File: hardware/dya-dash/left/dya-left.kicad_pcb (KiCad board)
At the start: 2 copper layers, 127.2 x 92.9 mm, 115 parts

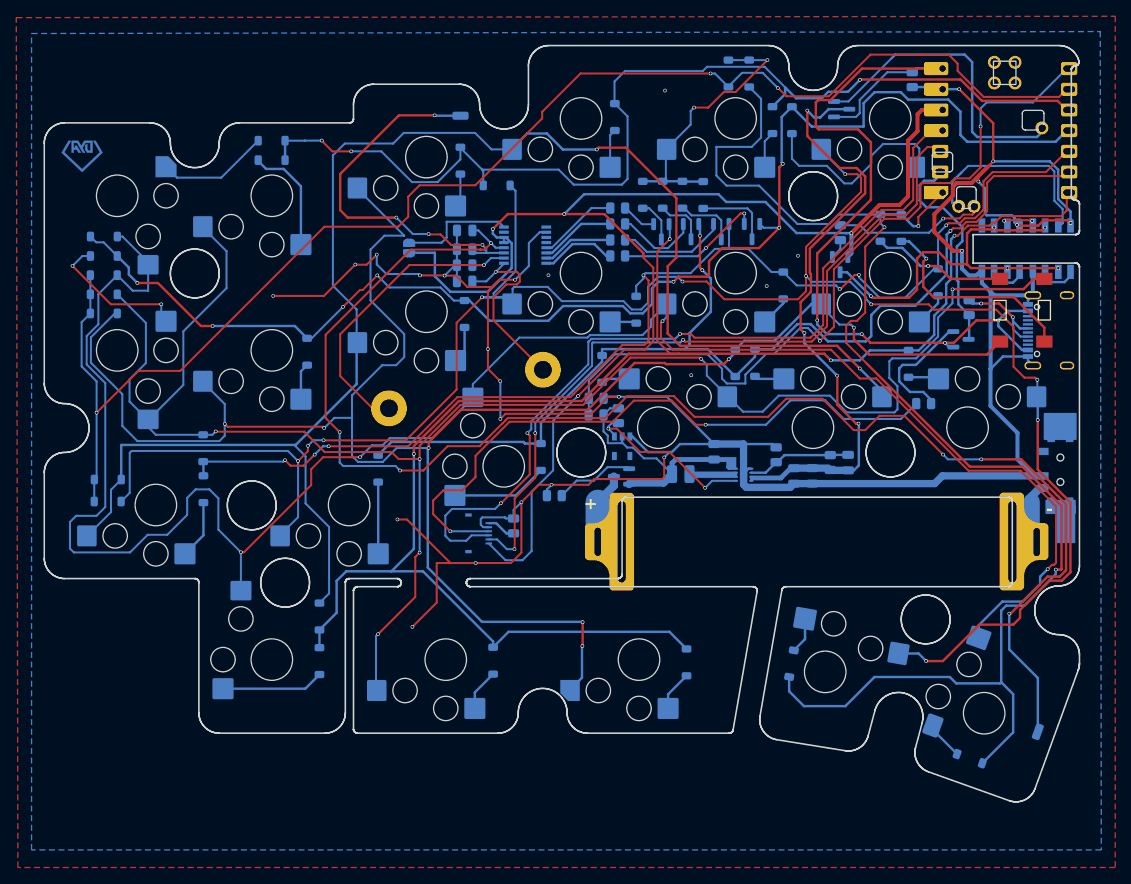
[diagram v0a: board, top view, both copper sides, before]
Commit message: Change FFC connector direction for arrow model
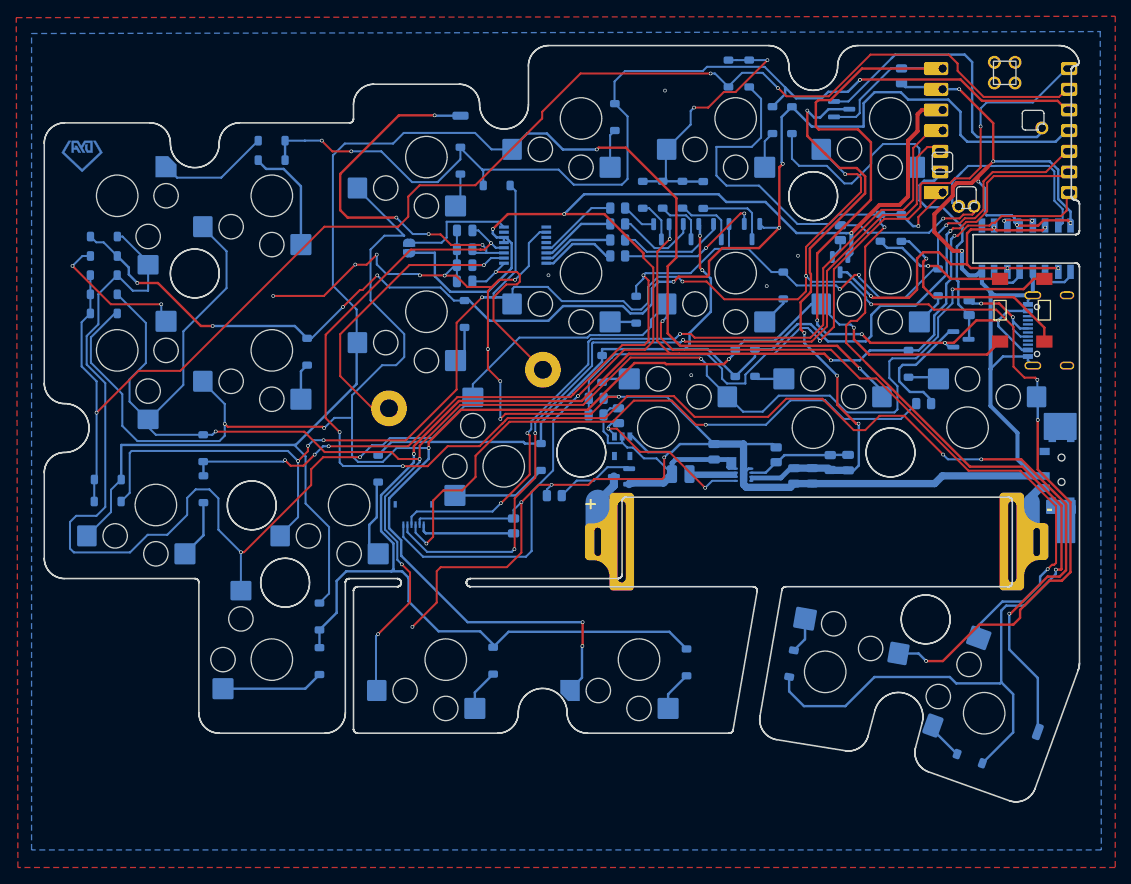
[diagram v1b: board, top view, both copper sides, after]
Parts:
- moved JL3 9.31 mm to (64.7, 77.0), turned to 0 degrees
- moved RL12 1.40 mm to (124.7, 21.9)
- moved SW_BATL1 0.14 mm to (144.4, 70.3)
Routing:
- net 3.3V_L: track 161.3 -> 173.3 mm
- net SCLK_L: track 93.7 -> 105.3 mm
- net Net-(JL3-Pin_6): track 3.56 -> 11.9 mm
- net Net-(DL28-A): track 237.2 -> 242.2 mm
- net GNDL: track 356.5 -> 352.1 mm, vias 27 -> 25
- net SDIO_L: track 102.8 -> 99.7 mm
- net PINL5: track 194.2 -> 197.0 mm
- net Net-(DL21-A): track 216.7 -> 219.2 mm
- net Net-(DL25-K): track 8.82 -> 9.72 mm
- net MOTION_L: track 79.6 -> 78.7 mm
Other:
- outline, holes or cut-outs redrawn
- board text added: "DYA Dash Rev2.2"
- board text removed: "DYA Dash Rev2.0"
